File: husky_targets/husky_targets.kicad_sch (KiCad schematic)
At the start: 25 parts, among them J1 HUSKEY_EDGE_CONNECTOR, J2 USB_C_Receptacle_USB2.0_16P, J3 Conn_01x04_Pin, U1 RP2350_60QFN, U2 W25Q128JVS

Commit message: finishing the schematic, starting with the layout
Signed-off-by: nitrogar <kernel101@yandex.com>
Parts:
- added C10: 2u2, Capacitor_SMD:C_0603_1608Metric_Pad1.08x0.95mm_HandSolder, symbol Device:C
- added C16, C21: 100n, Capacitor_SMD:C_0603_1608Metric_Pad1.08x0.95mm_HandSolder, symbol Device:C
- added J10, J11, J12, J5, J6, J7, J8, J9: Conn_01x01, Connector_PinHeader_1.27mm:PinHeader_1x01_P1.27mm_Vertical, symbol Connector_Generic:Conn_01x01
- added J4: Conn_01x02_Pin, Connector_PinHeader_1.27mm:PinHeader_1x02_P1.27mm_Vertical, symbol Connector:Conn_01x02_Pin
- added R10: 10, Resistor_SMD:R_0603_1608Metric_Pad0.98x0.95mm_HandSolder, symbol Device:R
- added R11: 3k3, Resistor_SMD:R_0603_1608Metric_Pad0.98x0.95mm_HandSolder, symbol Device:R
- added R12: 5k6, Resistor_SMD:R_0603_1608Metric_Pad0.98x0.95mm_HandSolder, symbol Device:R
- added R7: 1k, Resistor_SMD:R_0603_1608Metric_Pad0.98x0.95mm_HandSolder, symbol Device:R
- added R8, R9: 27, Resistor_SMD:R_0603_1608Metric_Pad0.98x0.95mm_HandSolder, symbol Device:R
- C1, C13, C14, C15, C19, C2, C20, C3, C4, C5, C6, C7, C8, C9: value C -> 100n; footprint (none) -> Capacitor_SMD:C_0603_1608Metric_Pad1.08x0.95mm_HandSolder
- R1, R2, R3: footprint (none) -> Resistor_SMD:R_0603_1608Metric_Pad0.98x0.95mm_HandSolder
- R4: value 5.11k -> 10; footprint (none) -> Resistor_SMD:R_0603_1608Metric_Pad0.98x0.95mm_HandSolder
- R5: value R -> DNF; footprint (none) -> Resistor_SMD:R_0603_1608Metric_Pad0.98x0.95mm_HandSolder
- R6: value R -> 0; footprint (none) -> Resistor_SMD:R_0603_1608Metric_Pad0.98x0.95mm_HandSolder
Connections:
- net FILT_LP is gone; now on net FILT_HP: J1.A3 (FILT_LP)
- net SHUNTH is gone; now on net FILT_HP: J1.B2 (SHUNTH)
- net SHUNTL is gone; now on net +3.3V: J1.B1 (SHUNTL)
- net VCC1.0 is gone; now on net +1V0: J1.B6 (VCC1.0)
- net +3.3V: now also U1.46 (VREG_AVDD), U1.49 (VREG_VIN), C10.1, C21.1, J5.1 (Pin_1), R10.1, R10.2, R12.2; no longer C13.1, C14.1, C15.1, U1.23 (DVDD), U1.39 (DVDD), U1.6 (DVDD)
- net CLIKIN: now also J7.1 (Pin_1)
- net D+: now also R8.2; no longer U1.51 (USB_DM)
- net D-: now also R9.2; no longer U1.52 (USB_DP)
- net GND: now also U1.47 (VREG_PGND), C10.2, C16.2, C21.2, J4.2 (Pin_2), R11.1
- net GPIO1/TX: now also J12.1 (Pin_1)
- net GPIO2/RX: now also J11.1 (Pin_1)
- net GPIO3: now also J10.1 (Pin_1)
- net GPIO4: now also J9.1 (Pin_1)
- net QSPI_SS: now also R7.1
- net nRST: now also J8.1 (Pin_1)
- net at U1.50 (VREG_FB): now also R11.2, R12.1
- net FILTIN renamed +1V0
- net +1V0: now also C13.1, C14.1, C15.1, U1.23 (DVDD), U1.39 (DVDD), U1.6 (DVDD), C16.1, J6.1 (Pin_1)
- new net: J4.1 (Pin_1), R7.2
- new net DN: R9.1, U1.51 (USB_DM)
- new net DP: R8.1, U1.52 (USB_DP)
- no-connect marks 26 -> 27
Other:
- moved on the sheet: C13, C14, C15, C7, C8, J3

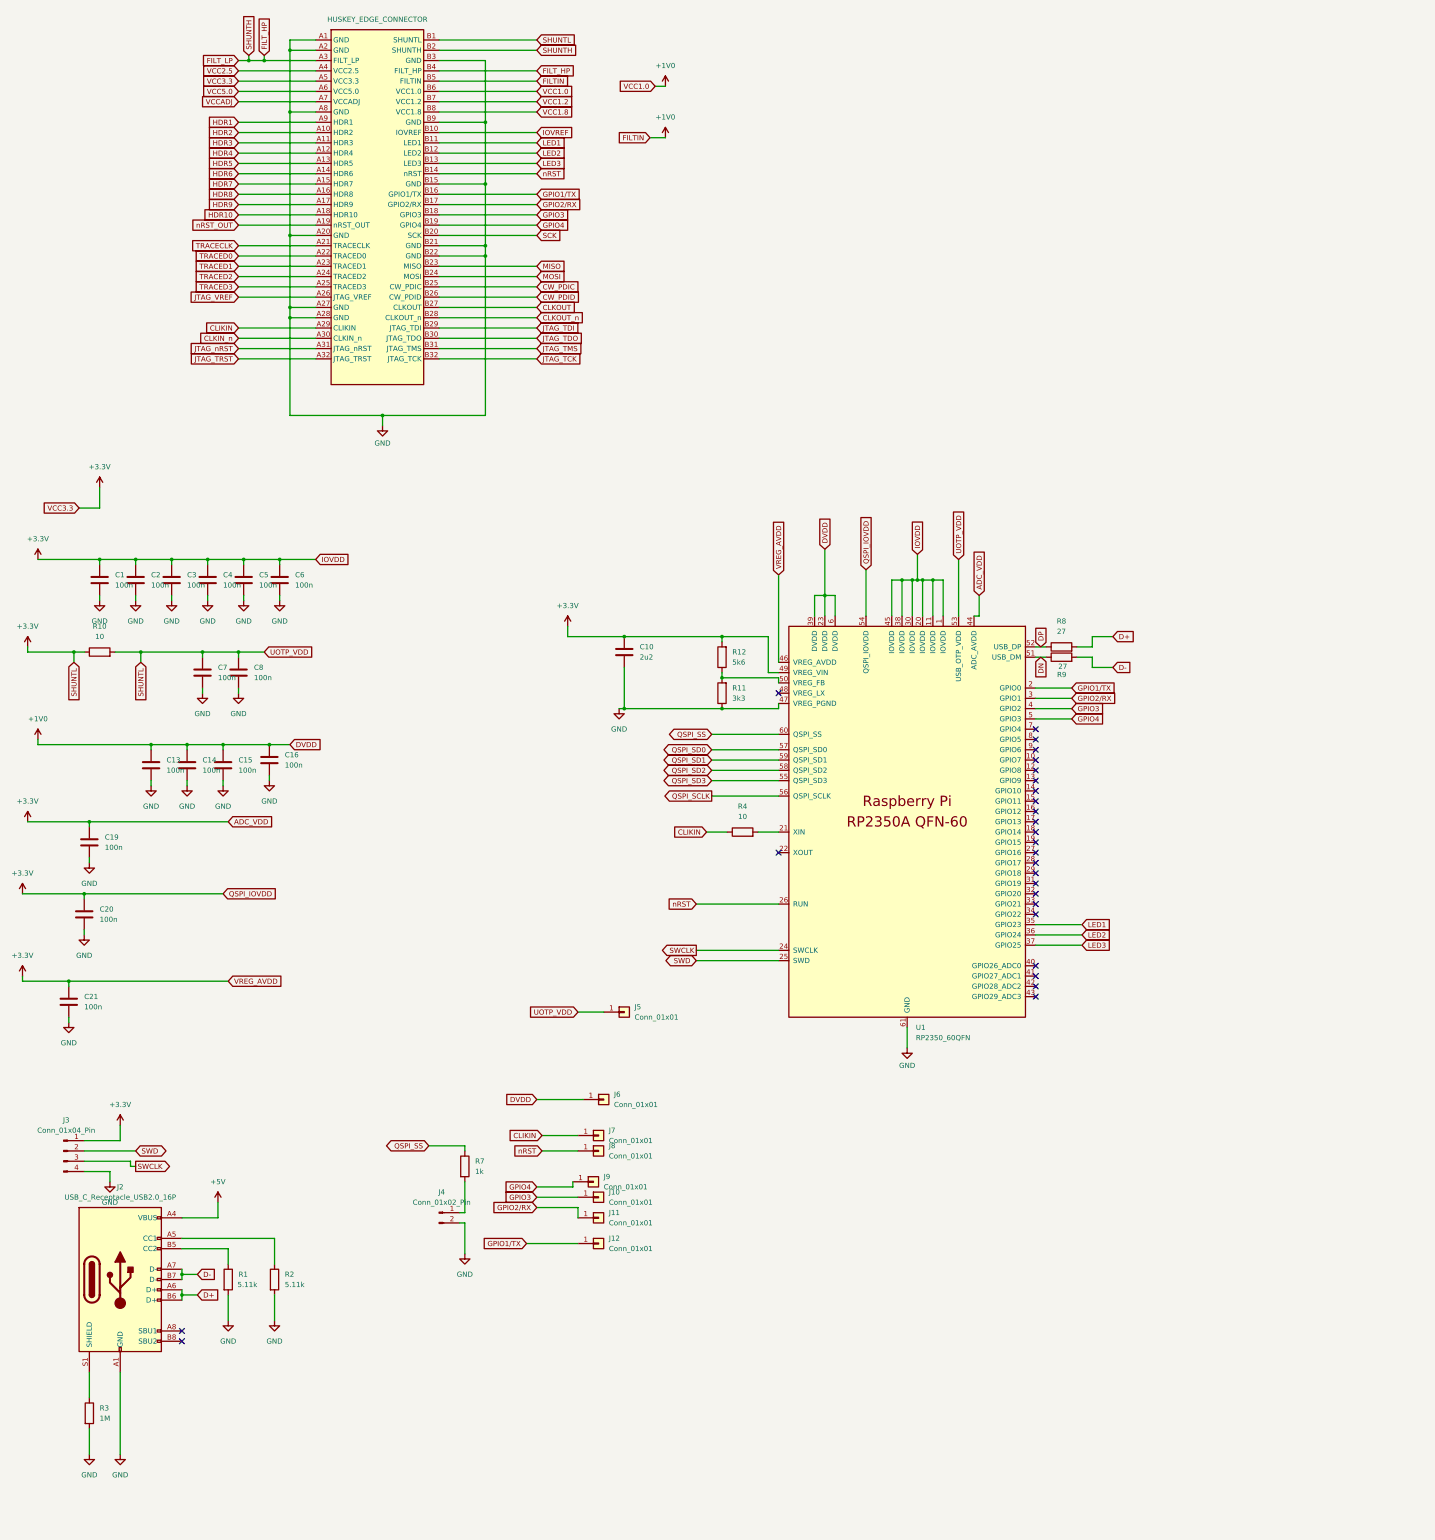
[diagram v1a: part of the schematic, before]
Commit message: done first version of RP2350 OTPVDD board
Signed-off-by: nitrogar <kernel101@yandex.com>
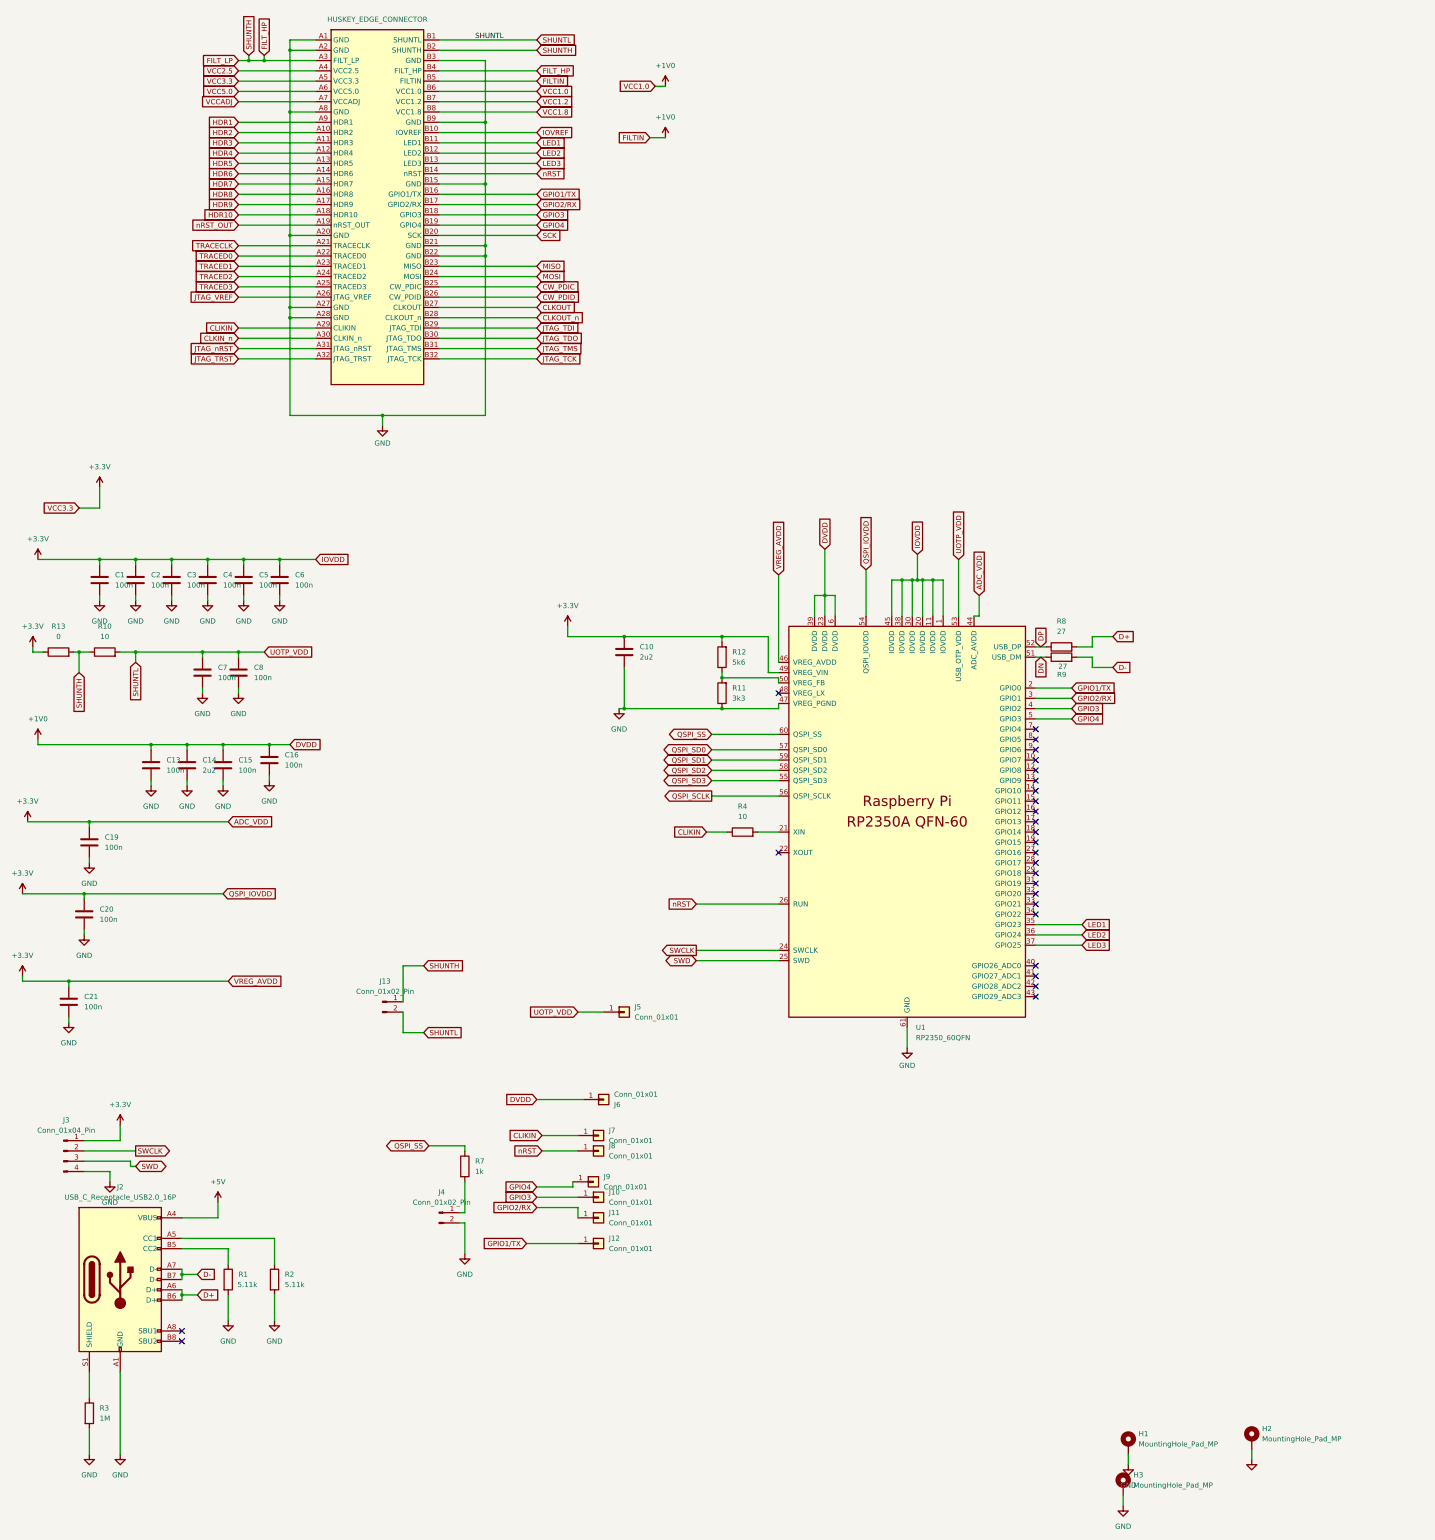
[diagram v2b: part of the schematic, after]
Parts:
- added H1, H2, H3: MountingHole_Pad_MP, MountingHole:MountingHole_2.2mm_M2_Pad_Via, symbol Mechanical:MountingHole_Pad_MP
- added J13: Conn_01x02_Pin, Connector_PinHeader_1.27mm:PinHeader_1x02_P1.27mm_Vertical, symbol Connector:Conn_01x02_Pin
- added R13: 0, Resistor_SMD:R_0603_1608Metric_Pad0.98x0.95mm_HandSolder, symbol Device:R
- C14: value 100n -> 2u2
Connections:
- net +3.3V: now also R13.1; no longer C7.1, C8.1, J1.B1 (SHUNTL), J5.1 (Pin_1), R10.1, R10.2, U1.53 (USB_OTP_VDD)
- net FILT_HP: now also R10.1, J13.1 (Pin_1), R13.2
- net GND: now also H1.MP, H2.MP, H3.MP
- net SWCLK: now also J3.2 (Pin_2); no longer J3.3 (Pin_3)
- net SWD: now also J3.3 (Pin_3); no longer J3.2 (Pin_2)
- new net SHUNTL: C7.1, C8.1, J1.B1 (SHUNTL), J13.2 (Pin_2), J5.1 (Pin_1), R10.2, U1.53 (USB_OTP_VDD)
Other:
- moved on the sheet: R10
